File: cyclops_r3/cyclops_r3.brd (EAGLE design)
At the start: 124.5 x 79.9 mm, 132 parts, among them Q1 BC817, Q2 IRF510, U1 MCP4921, U10 LMP7707, U11 ZXTD45, U12 ZXTD45, U2 ADG3301, U3 MCP4022-50k, U4 317-N, U5 TLV3701, U6 337L, U7 ADR03, U8 OP1177, U9 TLV2374, X1 SLP3, X2 SLP3, X3 SLP3

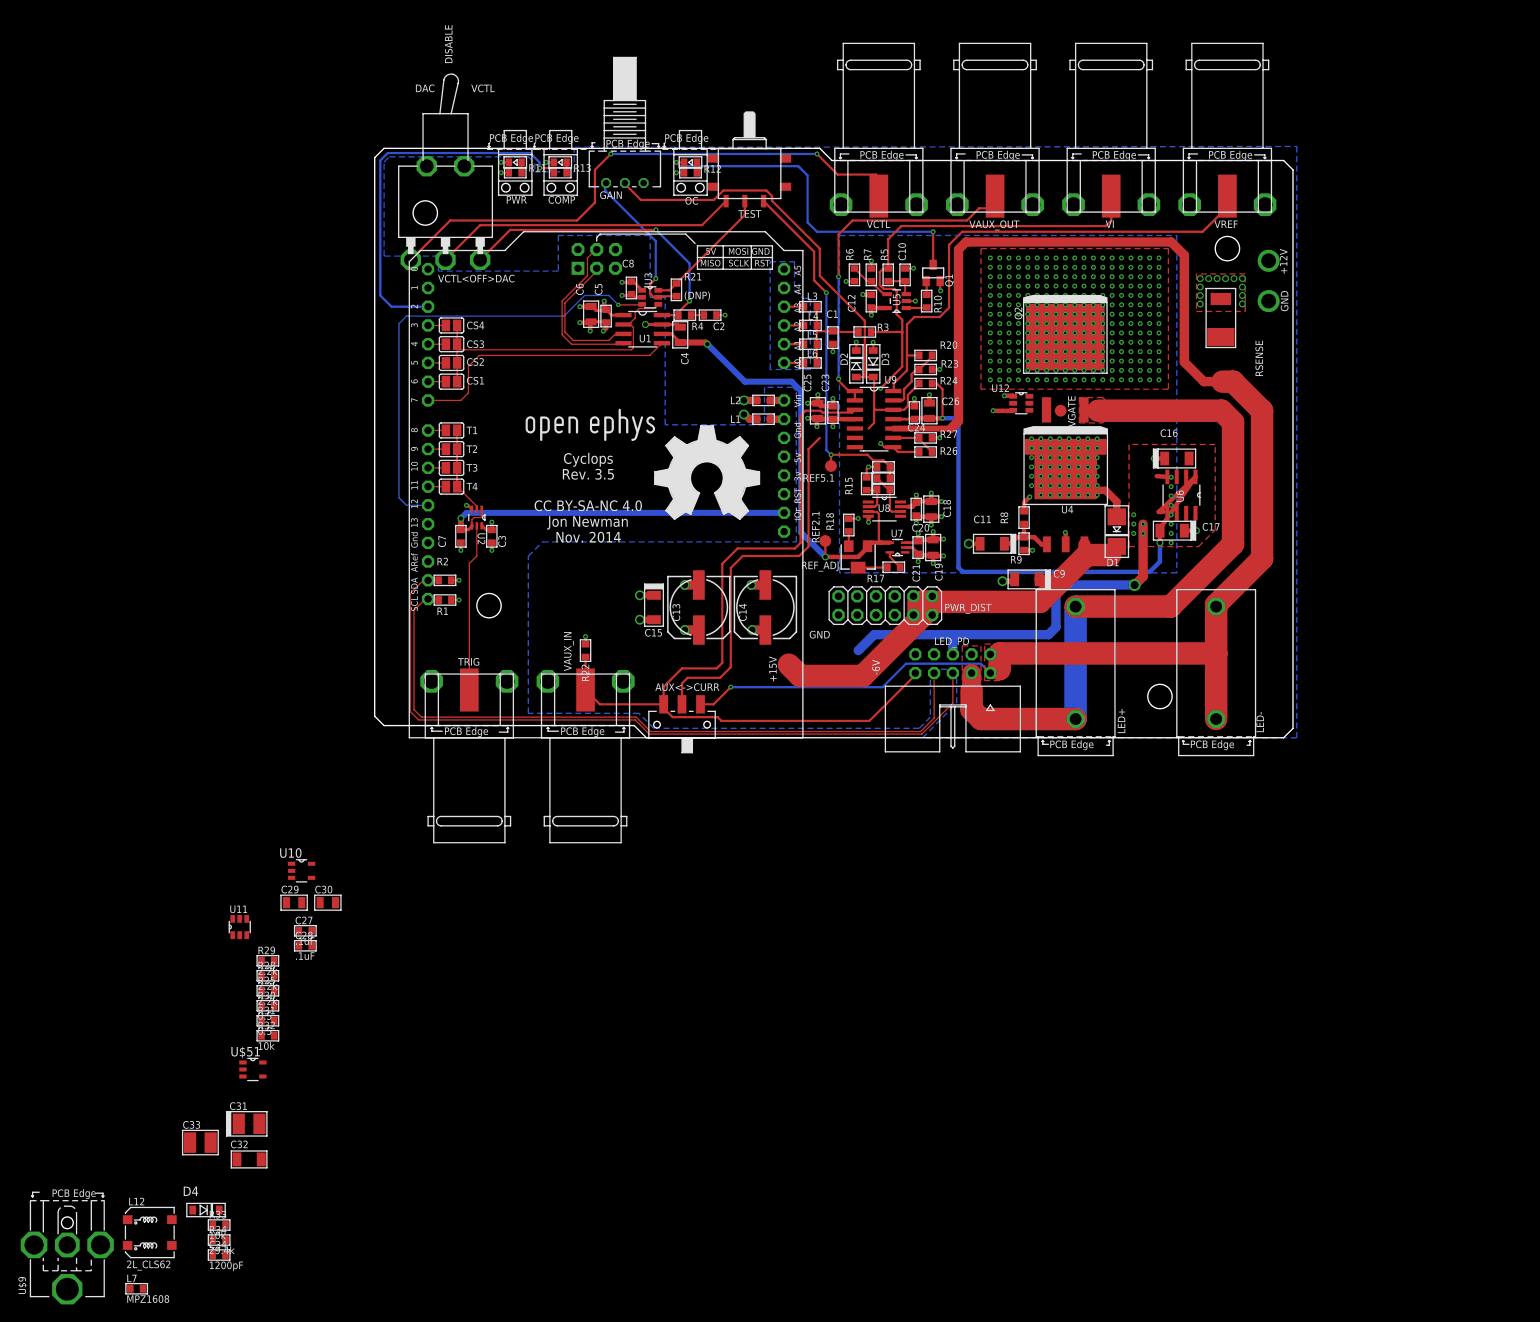
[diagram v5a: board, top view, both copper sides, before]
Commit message: Started laying out switching inverter.
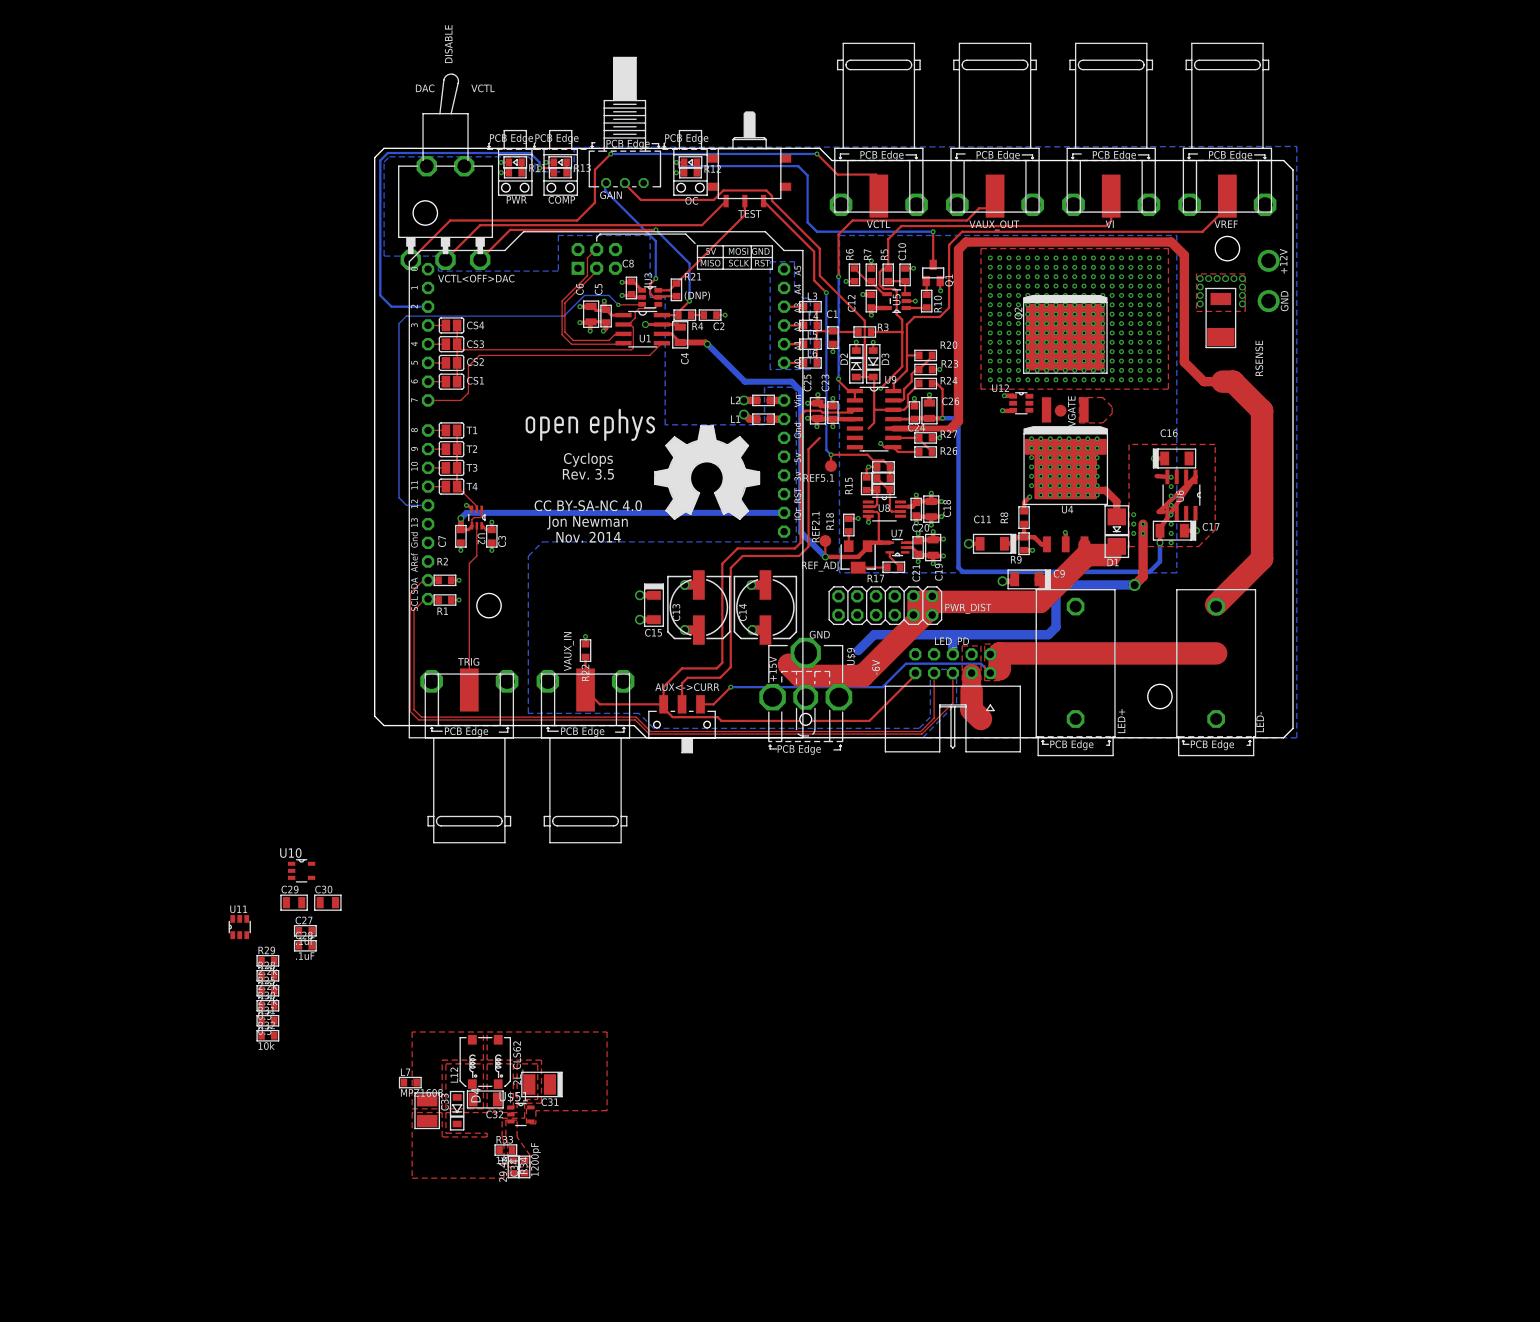
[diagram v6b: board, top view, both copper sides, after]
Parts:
- moved U$9 117.8 mm to (58.4, -0.51), turned to 180 degrees
- moved L12 51.0 mm to (15.0, -43.9), turned to 90 degrees
- moved L7 46.4 mm to (4.83, -46.7)
- moved C34 43.1 mm to (20.3, -58.2), turned to 90 degrees
- moved R34 41.1 mm to (18.8, -58.2), turned to 270 degrees
- moved R33 40.2 mm to (17.8, -55.9)
- moved C31 39.7 mm to (22.4, -47.0), turned to 180 degrees
- moved U$51 36.8 mm to (19.8, -51.1)
- moved D4 36.6 mm to (11.2, -50.5), turned to 270 degrees
- moved C32 33.0 mm to (15.0, -49.0), turned to 180 degrees
- moved C33 31.0 mm to (7.11, -50.5), turned to 270 degrees
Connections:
- net N$32: now also L12.2; no longer L12.1
- net N$33: now also L12.1; no longer L12.2
- net N$35: now also L12.4; no longer L12.3
- net VIN: now also L12.3; no longer L12.4
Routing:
- net LED+: track 95.1 -> 6.75 mm
- net LED-: track 213.3 -> 197.8 mm
- net -1.25V: track 86.4 -> 85.1 mm
- added copper zone on layer 1, net N$32
- added copper zone on layer 1, net N$33
- added copper zone on layer 1, net N$35
- added copper zone on layer 1, net N$36
- added copper zone on layer 1, net VIN

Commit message: Layout.
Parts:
- removed C29, C30: 1uF, cyclops:0805
- U$51: value LT1611 -> LT1931A
- moved R25 181.2 mm to (153.4, 33.8), turned to 270 degrees
- moved R32 141.3 mm to (98.6, 44.5), turned to 90 degrees
- moved R31 134.1 mm to (91.9, 43.2)
- moved R30 133.9 mm to (91.9, 45.0)
- moved R29 125.7 mm to (85.1, 46.5), turned to 180 degrees
- moved U11 124.0 mm to (84.3, 43.9), turned to 270 degrees
- moved R28 123.9 mm to (85.1, 41.4)
- moved C28 116.7 mm to (80.3, 46.5), turned to 180 degrees
- moved C27 112.3 mm to (80.3, 41.4)
- moved U10 109.2 mm to (80.0, 43.9), turned to 180 degrees
- moved C34 101.9 mm to (36.6, 42.4), turned to 180 degrees
- moved R34 100.6 mm to (36.6, 40.9), turned to 0 degrees
- moved R33 97.2 mm to (34.3, 39.9), turned to 90 degrees
- moved U$51 93.5 mm to (29.5, 41.9), turned to 90 degrees
- moved C31 91.5 mm to (25.4, 44.5), turned to 270 degrees
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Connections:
- removed net GND1: C27.2, C28.2, C29.2, C30.2
- net +11V: no longer C29.1
- net -1.25V: no longer C30.1
- net GND: now also C27.2, C28.2
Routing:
- net LED-: track 197.8 -> 173.2 mm
- net N$10: track 0.00 -> 7.49 mm
- net N$4: track 0.00 -> 7.44 mm
- net N$13: track 0.00 -> 4.46 mm
- net -1.25V: track 85.1 -> 83.6 mm, vias 3 -> 5
- net +11V: track 53.7 -> 52.5 mm, vias 344 -> 347

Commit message: Layout.
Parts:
- added C29, C30: 10nF, cyclops:0603
- added U$11: MAX4564, cyclops:SOT65P300X175-N
- moved C16 86.6 mm to (41.2, -16.3)
- moved C17 86.6 mm to (40.5, -26.0)
- moved U6 86.6 mm to (41.8, -21.2)
- moved C11 4.57 mm to (88.3, 26.3)
- moved D1 4.57 mm to (105.1, 27.9)
- moved R8 4.57 mm to (92.6, 29.8)
- moved R9 4.57 mm to (92.6, 26.3)
- moved U4 4.57 mm to (98.2, 33.4)
- moved C9 4.57 mm to (93.0, 21.5)
- moved C28 1.14 mm to (81.3, 47.0)
- moved R30 1.14 mm to (93.0, 45.5)
- moved R31 1.14 mm to (93.0, 43.7)
- moved U12 1.14 mm to (89.4, 44.5)
- moved C27 1.14 mm to (81.3, 41.9)
- moved R29 1.14 mm to (86.1, 47.0)
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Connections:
- removed net VFB: AUX<->CURR.2, U10.4
- new net -1.15V: C29.1, U$11.3
- new net COM: U$11.1, U10.4
- new net IN: AUX<->CURR.2, U$11.5
- net +11V: now also AUX<->CURR.1, C30.1, U$11.8
- net GND: now also AUX<->CURR.3, C29.2, C30.2, U$11.2, U$11.4
- net LED-: now also U$11.7; no longer AUX<->CURR.3
- net VAUX: now also U$11.6; no longer AUX<->CURR.1
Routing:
- net -1.25V: track 83.6 -> 21.8 mm, vias 5 -> 3
- net -5V: track 55.2 -> 0.00 mm, vias 14 -> 12
- net VFB: track 50.9 -> 0.00 mm
- net VAUX: track 116.0 -> 104.5 mm
- net +15V: track 67.5 -> 72.1 mm
- net LED-: track 173.2 -> 171.1 mm
